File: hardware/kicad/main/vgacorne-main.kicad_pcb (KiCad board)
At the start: 2 copper layers, 134.4 x 93.5 mm, 135 parts, among them J1 TYPE-C-31-M-12, J2 SWD, J3 SM10B-SRSS-TB, J4 MCU module, SW1 C0R0, SW10 C3R0, SW11 C3R1, SW12 C3R2, SW13 C4R0, SW14 C4R1, SW15 C4R2, SW16 C5R0, SW17 C5R1, SW18 C5R2, SW19 T0, SW2 C0R1, SW20 T1, SW21 T2, SW22 BOOT, SW23 RESET, SW3 C0R2, SW4 C1R0, SW5 C1R1, SW6 C1R2, SW7 C2R0, SW8 C2R1, SW9 C2R2, U11 SN74LV4051APWR, U12 SN74LV4051APWR, U13 SN74LV4051APWR, U2 TLV75733PDBVR, U3 XC6206P332MR, U4 USBLC6-2SC6, U6 SRV05-4, U7 SRV05-4

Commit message: Add trackpad, mouse column and scroll wheel; move MCU and ports
Layout
- MCU module, USB-C and trackpad move to the right half; the left half
  is now the passive satellite.
- VGA daughterboard bay moves to the inner-back corner so both cables
  leave from the back face. The bay sits 4.5 mm further back than the
  keys need, so both halves are 116 mm deep.
- Azoteq TPS65 trackpad, landscape, right beside Y/H/N under a 1 mm
  overlay. The MCU module moves to a PCB ear behind it, next to the
  VGA bay. trackpad.py selects the pad (TPS65 or 40 mm Cirque); the
  case pocket, J5 connector and QMK driver follow the selection.
- Left half: a mouse column beside T/G/B with a scroll wheel (Bourns
  PEC12R) at the top and left/right-click HE keys beside G and B.

Circuits and firmware
- Mux channels reassigned so the satellite's mouse keys and wheel fill
  its three spare channels. The wheel's A/B contacts are summed into
  four voltage levels on one channel.
- QMK: 44-key LAYOUT and a wheel decoder that feeds QMK's quadrature
  encoder driver. Trackpad on I2C1, with rules.mk now generated. The
  host test covers the wheel.
- libhmk: MS_BTN1/MS_BTN2 on the mouse keys (no encoder support).

Case and renders
- Smoother milled case: 7.25 mm walls, 25 mm minimum outside radius
  and a flat back face at the ports.
- render.py builds Blender Cycles renders from the design geometry.

Co-Authored-By: Claude Opus 5.5 (1M context) <noreply@anthropic.com>
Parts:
- added C16: 1u, Capacitor_SMD:C_0603_1608Metric, B.Cu at (139.6, 47.2)
- added C17: 100n, Capacitor_SMD:C_0402_1005Metric, B.Cu at (142.2, 48.9)
- added J5: Trackpad, Connector_FFC-FPC:Jushuo_AFC07-S06FCA-00_1x6-1MP_P0.50_Horizontal, F.Cu at (141.1, 47.2)
- added R19: 4.7k, Resistor_SMD:R_0402_1005Metric, B.Cu at (141.1, 47.2)
- added R20: 4.7k, Resistor_SMD:R_0402_1005Metric, B.Cu at (142.6, 47.2)
- moved C201 257.2 mm to (281.2, 52.1)
- moved C202 257.2 mm to (281.2, 71.1)
- moved C203 257.2 mm to (281.2, 90.2)
- moved HE1 257.2 mm to (278.6, 52.9)
- moved HE2 257.2 mm to (278.6, 71.9)
- moved HE3 257.2 mm to (278.6, 91.0)
- moved SW1 257.2 mm to (278.6, 52.9)
- moved SW2 257.2 mm to (278.6, 71.9)
- moved SW3 257.2 mm to (278.6, 91.0)
- moved C101 257.2 mm to (276.0, 52.1)
- moved C102 257.2 mm to (276.0, 71.1)
- moved C103 257.2 mm to (276.0, 90.2)
- moved H1 238.1 mm to (269.1, 62.4)
- moved H2 238.1 mm to (269.1, 81.4)
- moved HE4 219.1 mm to (259.5, 52.9)
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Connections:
- J4 pad 1: GND -> /I2C_SCL
- J4 pad 2: GND -> /I2C_SDA
- U11 pad 2: GND -> /HE_C2R0
- U11 pad 4: GND -> /HE_C2R1
- U12 pad 1: /HE_C3R1 -> /HE_C4R0
- U12 pad 12: /HE_C3R0 -> /HE_C3R2
- U12 pad 13: /HE_C2R0 -> /HE_C2R2
- U12 pad 14: /HE_C2R1 -> /HE_C3R0
- U12 pad 15: /HE_C2R2 -> /HE_C3R1
- U12 pad 2: /HE_T0 -> /HE_C4R2
- U12 pad 4: GND -> /HE_T0
- U12 pad 5: /HE_C3R2 -> /HE_C4R1
- U13 pad 1: /HE_C5R1 -> /HE_T2
- U13 pad 12: /HE_C5R0 -> /HE_T1
- U13 pad 13: /HE_C4R0 -> /HE_C5R0
- U13 pad 14: /HE_C4R1 -> /HE_C5R1
- U13 pad 15: /HE_C4R2 -> /HE_C5R2
- U13 pad 2: /HE_T1 -> GND
- U13 pad 4: /HE_T2 -> GND
- U13 pad 5: /HE_C5R2 -> GND
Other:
- board size 134.4 x 93.5 mm -> 154.9 x 105.9 mm
- board text added: "VGACorne right rev 0.1"
- board text removed: "VGACorne left rev 0.1"

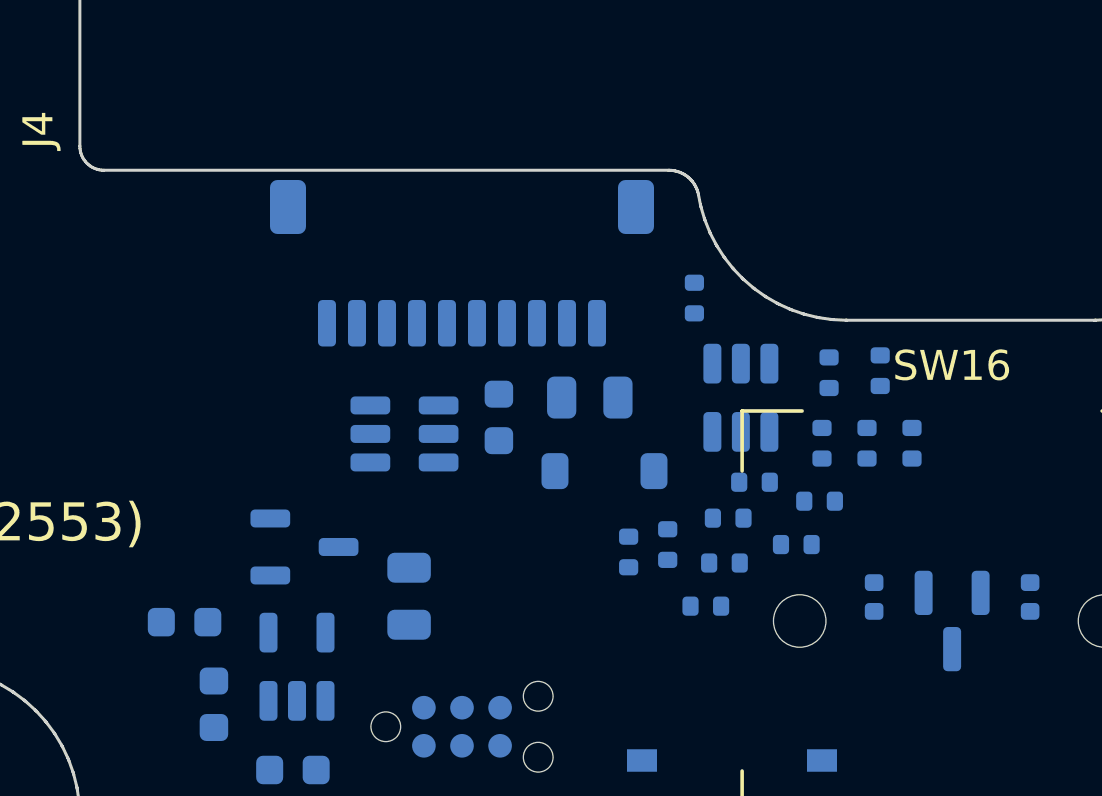
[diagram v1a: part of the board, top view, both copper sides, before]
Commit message: Replace the scroll wheel with a rotary encoder knob
The left half's mouse column now runs, top to bottom: right click beside
T, left click beside G, and a rotary encoder with a knob beside B, all
in line with column 5's rows.
- Encoder: Bourns PEC12R-4220F-N0024 (upright, 20 mm shaft, 24
  detents, no switch). It sits in a normal 14 mm plate cutout, which
  replaces the wheel notch. The knob is 16 mm across.
- Same readout as before: the A/B contacts are summed into four levels
  on the satellite's last spare mux channel. Nets, QMK defines and code
  are renamed from wheel to encoder (ENC, HE_ENCODER_*).
- The link connector J3 goes back to its original spot, now that the
  encoder legs are elsewhere.
- Docs, BOM, PCB images and renders regenerated.

Co-Authored-By: Claude Opus 5.5 (1M context) <noreply@anthropic.com>
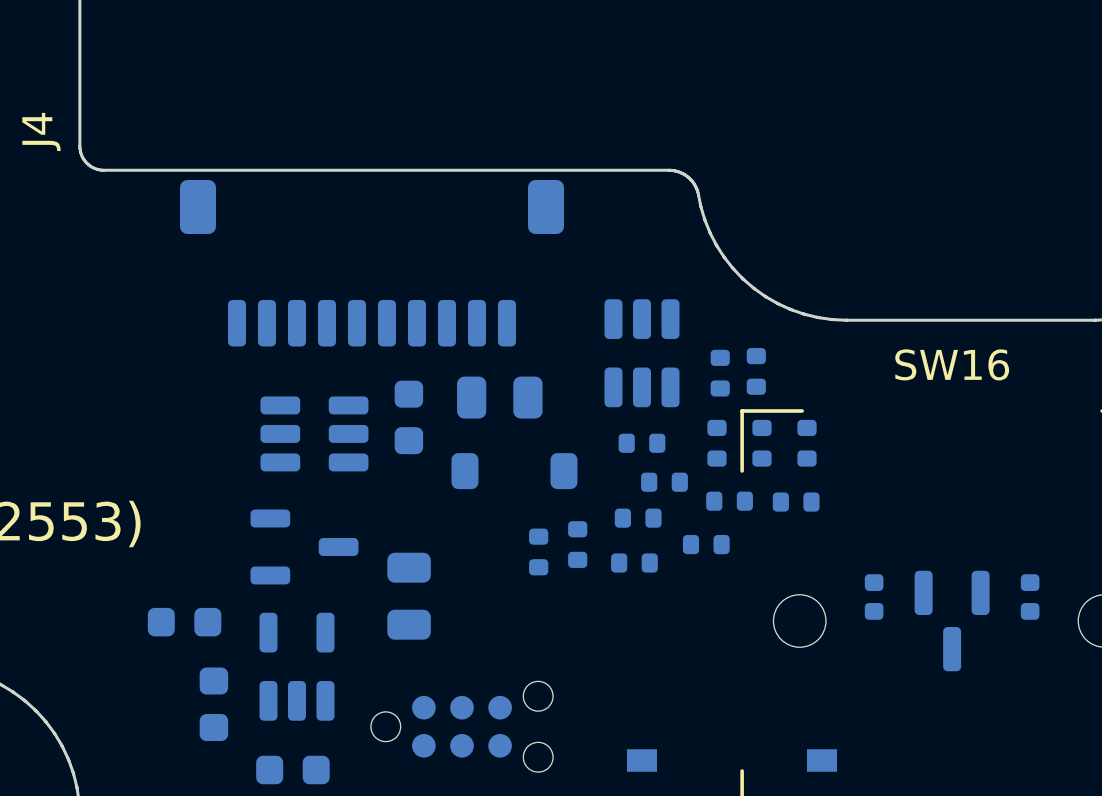
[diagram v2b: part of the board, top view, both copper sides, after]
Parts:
- moved R13 8.72 mm to (172.7, 48.5), turned to 0 degrees
- moved R12 7.04 mm to (175.1, 47.9), turned to 0 degrees
- moved R10 6.33 mm to (175.6, 42.2), turned to -90 degrees
- moved R8 6.07 mm to (172.9, 47.0)
- moved R16 5.86 mm to (169.6, 48.2), turned to -90 degrees
- moved R11 4.61 mm to (177.0, 44.5)
- moved R18 4.33 mm to (178.1, 46.5), turned to 0 degrees
- moved R5 3.97 mm to (173.0, 44.5)
- moved U6 3.61 mm to (173.0, 41.5)
- moved R7 3.50 mm to (175.5, 44.5)
- moved R17 3.44 mm to (178.5, 44.5)
- moved R15 3.20 mm to (176.8, 42.2)
- moved C15 3.00 mm to (165.2, 43.7)
- moved D1 3.00 mm to (168.7, 45.5)
- moved F2 3.00 mm to (168.3, 43.0)
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
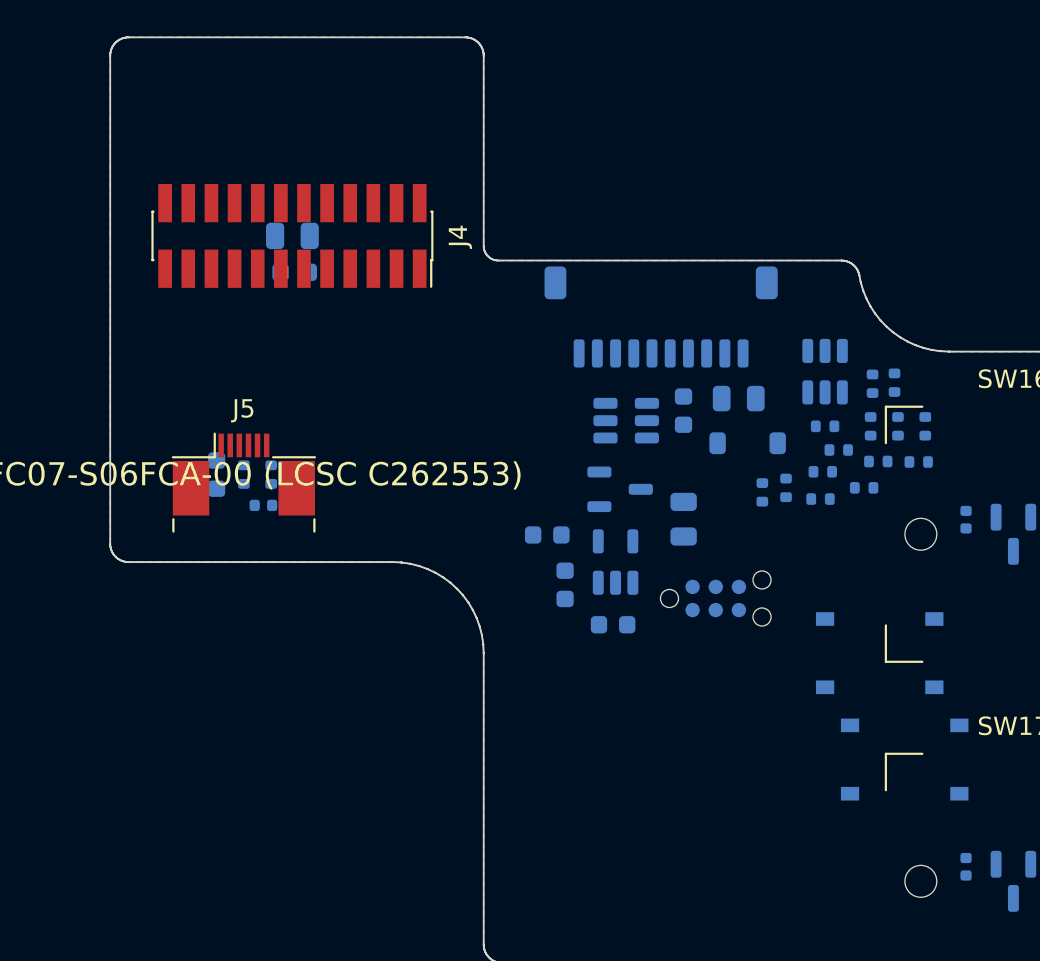
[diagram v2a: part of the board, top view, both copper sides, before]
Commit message: Solder the MCU module flat under the trackpad
The plug-in module stood 8 mm tall on a 2x12 socket, on a PCB ear
behind the trackpad that reached back to the rear face. That kept the
right half's back edge straight across most of the trackpad.

It is now a castellated stamp module:
- 19.4 x 25 mm, with 2x12 half-holes at 1.27 mm and every part on top.
- Soldered onto landing pads J4 on the main PCB's tab, beside Y/H/N,
  under the trackpad.
- About 2.7 mm tall: 1.6 mm below the TPS65's well, 2.2 mm below the
  Cirque's.

With the ear gone, a small PCB tongue under the pad carries its FFC
connector J5. The case back now tapers right from the keys; size and
port positions are unchanged.

- New footprints: castellated module edge and matching landing pads.
- Module boards: all parts on top; a label on the flat underside.
- checks.module_connector now compares castellated hole positions with
  landing pad centres.
- Stack-up: module height and clearance are measured against the
  trackpad well.
- Parts can opt out of the BOM (the module's edge pads are not a part).
- Docs, BOM and images regenerated.

Co-Authored-By: Claude Opus 5.5 (1M context) <noreply@anthropic.com>
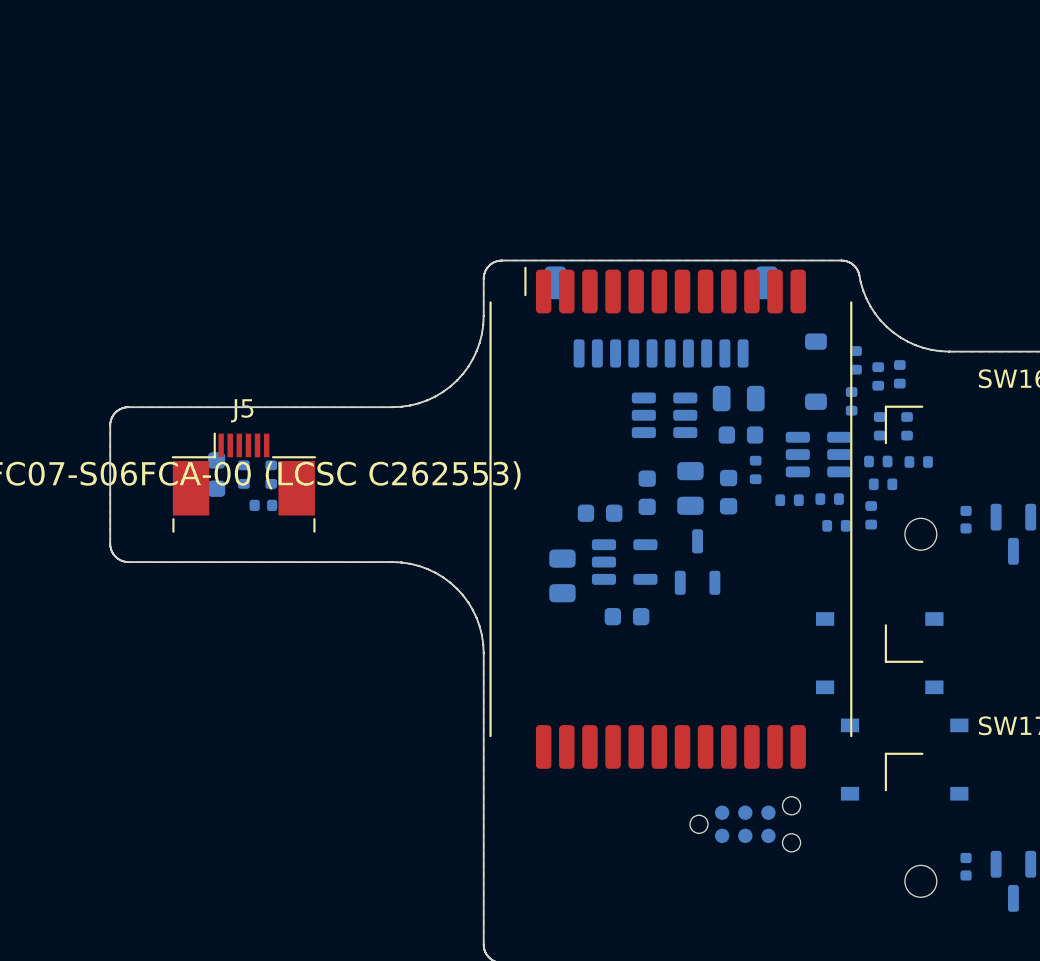
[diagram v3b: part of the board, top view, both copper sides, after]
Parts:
- J4: footprint Connector_PinSocket_1.27mm:PinSocket_2x12_P1.27mm_Vertical_SMD -> vgacorne:Module_Castellated_Landing_2x12_P1.27mm_19.4x25mm
- moved C10 26.7 mm to (167.7, 48.2), turned to 90 degrees
- moved J4 26.0 mm to (164.5, 49.6), turned to 0 degrees
- moved C9 25.9 mm to (165.6, 48.0), turned to 90 degrees
- moved J2 12.5 mm to (168.6, 66.4)
- moved U7 10.7 mm to (172.6, 46.1)
- moved U6 9.13 mm to (164.2, 43.9), turned to 0 degrees
- moved R16 8.74 mm to (178.1, 46.5), turned to 0 degrees
- moved C4 7.34 mm to (158.6, 52.8)
- moved C5 5.95 mm to (163.2, 48.2), turned to 90 degrees
- moved U3 5.83 mm to (166.0, 52.0), turned to 90 degrees
- moved R18 5.72 mm to (173.6, 50.0)
- moved R17 5.72 mm to (175.5, 49.4)
- moved R9 5.68 mm to (174.7, 40.9), turned to -90 degrees
- moved D1 5.43 mm to (172.5, 41.5), turned to 90 degrees
- moved C3 4.37 mm to (160.6, 49.3), turned to 0 degrees
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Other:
- outline, holes or cut-outs redrawn

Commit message: Fix design audit findings
Electrical:
- Re-map the castellated module's pads so neighbours on each edge follow
  the LQFP: USB D+/D- together between grounds at the corner nearest the
  USB-C, the six ADC inputs grouped beside +3.3VA, a ground away from the
  select lines.
- Put 1k between each DRV5055 output and its 4.7n cap (TI: no capacitor
  straight on the output).
- STM32F446 module: pull PB2/BOOT1 down so BOOT reaches DFU; pull PA10 up.
- Replace the XC6206 with a second TLV75733, and the link polyfuse with a
  TPS2051C switch (soft start, current limit) so hot-plugging the satellite
  can't brown out the MCU. F1 is now 750 mA.
- USB net class 0.4/0.15 mm: ~97 ohm differential against the pour on both
  2-layer boards (was ~120).
- BOM gains a Tolerance column; part numbers for the F446 crystal.

Mechanical:
- Case foam 2 mm, leaving 0.5 mm under the bottom-side parts (the old stack
  pressed the foam into every sensor).
- USB-C overhangs the ear by 0.46 mm and the opening takes a spec-maximum
  overmould (13.95 x 8.1 mm); the old 11 x 6 mm stopped most plugs short.
- DE-15 rear-mount cutout 20.5 x 11.4 mm; floor pockets under the USB-C and
  encoder pins; plate foam clears the module and the encoder's pins.
- Knob 11.5 mm tall so it clears the encoder's collar.

Docs, PCB images and renders updated to match.

Co-Authored-By: Claude Opus 5.5 (1M context) <noreply@anthropic.com>
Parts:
- removed F2: 500mA, Fuse:Fuse_0805_2012Metric
- added C18: 100n, Capacitor_SMD:C_0402_1005Metric, B.Cu at (166.1, 43.2)
- added R301: 1k, Resistor_SMD:R_0402_1005Metric, B.Cu at (281.2, 54.2)
- added R302: 1k, Resistor_SMD:R_0402_1005Metric, B.Cu at (281.2, 73.3)
- added R303: 1k, Resistor_SMD:R_0402_1005Metric, B.Cu at (281.2, 92.3)
- added R304: 1k, Resistor_SMD:R_0402_1005Metric, B.Cu at (262.1, 54.2)
- added R305: 1k, Resistor_SMD:R_0402_1005Metric, B.Cu at (262.1, 73.3)
- added R306: 1k, Resistor_SMD:R_0402_1005Metric, B.Cu at (262.1, 92.3)
- added R307: 1k, Resistor_SMD:R_0402_1005Metric, B.Cu at (243.1, 49.4)
- added R308: 1k, Resistor_SMD:R_0402_1005Metric, B.Cu at (243.1, 68.5)
- added R309: 1k, Resistor_SMD:R_0402_1005Metric, B.Cu at (243.1, 87.5)
- added R310: 1k, Resistor_SMD:R_0402_1005Metric, B.Cu at (224.0, 47.1)
- added R311: 1k, Resistor_SMD:R_0402_1005Metric, B.Cu at (224.0, 66.1)
- added R312: 1k, Resistor_SMD:R_0402_1005Metric, B.Cu at (224.0, 85.2)
- added R313: 1k, Resistor_SMD:R_0402_1005Metric, B.Cu at (205.0, 49.4)
- added R314: 1k, Resistor_SMD:R_0402_1005Metric, B.Cu at (205.0, 68.5)
- added R315: 1k, Resistor_SMD:R_0402_1005Metric, B.Cu at (205.0, 87.5)
- added R316: 1k, Resistor_SMD:R_0402_1005Metric, B.Cu at (185.9, 51.8)
- added R317: 1k, Resistor_SMD:R_0402_1005Metric, B.Cu at (185.9, 70.9)
- added R318: 1k, Resistor_SMD:R_0402_1005Metric, B.Cu at (185.9, 89.9)
- added R319: 1k, Resistor_SMD:R_0402_1005Metric, B.Cu at (214.5, 109.0)
- added R320: 1k, Resistor_SMD:R_0402_1005Metric, B.Cu at (193.9, 110.6)
- added R321: 1k, Resistor_SMD:R_0402_1005Metric, B.Cu at (169.1, 114.8)
- added U8: TPS2051CDBVR, Package_TO_SOT_SMD:SOT-23-5, B.Cu at (168.9, 43.9)
- F1: value 500mA -> 750mA
- U3: value XC6206P332MR -> TLV75733PDBVR; footprint Package_TO_SOT_SMD:SOT-23-3 -> Package_TO_SOT_SMD:SOT-23-5
- moved U7 11.2 mm to (161.5, 44.3), turned to 90 degrees
- moved R15 9.38 mm to (171.7, 49.4)
- moved U6 9.33 mm to (173.3, 46.2)
- moved R14 9.13 mm to (178.0, 44.5)
- moved C1 8.23 mm to (198.1, 33.7)
- moved R18 6.13 mm to (178.7, 46.5)
- moved F1 5.61 mm to (203.4, 36.6), turned to 0 degrees
- moved R16 4.93 mm to (177.1, 41.7), turned to -90 degrees
- moved R11 4.79 mm to (175.0, 48.6), turned to 0 degrees
- moved C15 3.96 mm to (164.5, 44.4), turned to 90 degrees
- moved R12 3.44 mm to (173.0, 49.0), turned to -90 degrees
- moved R8 2.94 mm to (170.5, 47.6), turned to -90 degrees
- moved R13 2.49 mm to (169.2, 46.9), turned to -90 degrees
- moved R17 2.48 mm to (177.4, 47.8), turned to 0 degrees
- moved R7 0.59 mm to (176.5, 46.5)
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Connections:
- HE1 pad 2: /HE_C0R0 -> /HE_C0R0_OUT
- HE10 pad 2: /HE_C3R0 -> /HE_C3R0_OUT
- HE11 pad 2: /HE_C3R1 -> /HE_C3R1_OUT
- HE12 pad 2: /HE_C3R2 -> /HE_C3R2_OUT
- HE13 pad 2: /HE_C4R0 -> /HE_C4R0_OUT
- HE14 pad 2: /HE_C4R1 -> /HE_C4R1_OUT
- HE15 pad 2: /HE_C4R2 -> /HE_C4R2_OUT
- HE16 pad 2: /HE_C5R0 -> /HE_C5R0_OUT
- HE17 pad 2: /HE_C5R1 -> /HE_C5R1_OUT
- HE18 pad 2: /HE_C5R2 -> /HE_C5R2_OUT
- HE19 pad 2: /HE_T0 -> /HE_T0_OUT
- HE2 pad 2: /HE_C0R1 -> /HE_C0R1_OUT
- HE20 pad 2: /HE_T1 -> /HE_T1_OUT
- HE21 pad 2: /HE_T2 -> /HE_T2_OUT
- HE3 pad 2: /HE_C0R2 -> /HE_C0R2_OUT
- HE4 pad 2: /HE_C1R0 -> /HE_C1R0_OUT
- HE5 pad 2: /HE_C1R1 -> /HE_C1R1_OUT
- HE6 pad 2: /HE_C1R2 -> /HE_C1R2_OUT
- HE7 pad 2: /HE_C2R0 -> /HE_C2R0_OUT
- HE8 pad 2: /HE_C2R1 -> /HE_C2R1_OUT
- HE9 pad 2: /HE_C2R2 -> /HE_C2R2_OUT
- J4 pad 1: /I2C_SCL -> /NRST
- J4 pad 10: GND -> +3.3VA
- J4 pad 11: /ADC_L_A -> +3V3
- J4 pad 12: /ADC_L_B -> /ADC_L_A
- J4 pad 13: /ADC_L_C -> /SWCLK
- J4 pad 14: /ADC_R_A -> /ADC_L_B
- J4 pad 15: /ADC_R_B -> /SWDIO
- J4 pad 16: /ADC_R_C -> /ADC_L_C
- J4 pad 17: /MUX_S0 -> GND
- J4 pad 18: /MUX_S1 -> /ADC_R_A
- J4 pad 19: /MUX_S2 -> /USB_DP
- J4 pad 2: /I2C_SDA -> /MUX_S0
- J4 pad 20: /DET -> /ADC_R_B
- J4 pad 21: /NRST -> /USB_DN
- J4 pad 22: /BOOT -> /ADC_R_C
- J4 pad 23: /SWDIO -> GND
- J4 pad 24: /SWCLK -> /DET
- J4 pad 3: +3V3 -> /BOOT
- J4 pad 4: +3.3VA -> /MUX_S1
- J4 pad 5: +5V -> /I2C_SDA
- J4 pad 6: GND -> /MUX_S2
- J4 pad 7: /USB_DP -> /I2C_SCL
- J4 pad 8: /USB_DN -> GND
- J4 pad 9: GND -> +5V
- U3 pad 1: GND -> +5V
- U3 pad 2: +3V3 -> GND

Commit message: Route the VGA daughterboard with Freerouting
hardware/route.py drives Freerouting directly (the KiCad MCP's autorouter
trips over a pcbnew/Python 3.14 binding bug): signals first with the
ground pours as planes, then ground as tracks round the locked signals,
then the pours and ground stitching vias. The daughterboard routes
completely and passes DRC.

To make it routable:
- the 10-pin link order now follows the DE-15 under the pigtail pads
  (J3 on both halves follows; the pigtail stays 1:1, +5 V on pin 1);
- the pigtail pads are shorter and at the board edge, leaving a via
  channel above the connector;
- the socket keeps KiCad's 1.6 mm pads round Amphenol's 1.2 mm holes,
  so a track fits between pins;
- both cable-variant jumpers sit together by pins 9 and 15.

generate.py --force pcbs now leaves boards with tracks alone.

Co-Authored-By: Claude Opus 5.5 (1M context) <noreply@anthropic.com>
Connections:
- J3 pad 10: /LINK_C -> GND
- J3 pad 2: GND -> /LINK_DET
- J3 pad 3: /LINK_S0 -> /LINK_S1
- J3 pad 4: /LINK_S1 -> /LINK_S0
- J3 pad 6: /LINK_DET -> /LINK_C
- J3 pad 7: GND -> /LINK_B
- J3 pad 9: /LINK_B -> GND
